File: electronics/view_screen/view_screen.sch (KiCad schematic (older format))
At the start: 12 parts, among them J1 Conn_01x04, J2 GC9A01, J3 Conn_01x04, J4 Conn_01x04, J5 Conn_01x04, Q1 2N7002

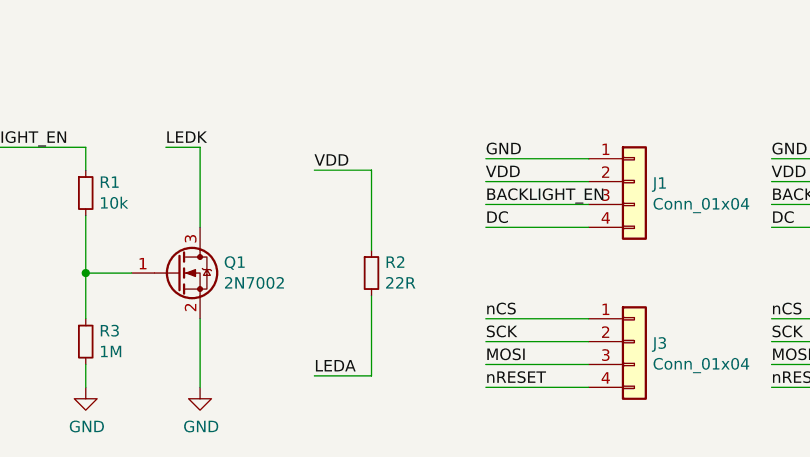
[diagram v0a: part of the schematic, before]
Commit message: Generate PCB assembly files
Generate assembly files for JLCPCB - BOM and CPL. Using existing LCSC part numbers (which may not be in the JLC part library), and positions/rotations are completely unverified, and of course many of the components are simply not available in any form in the JLC part library (e.g. TMC6300). Fixes #23.

Also changed LCD backlight resistor from 22 ohm to 20 ohm and added some additional part numbers for reference.
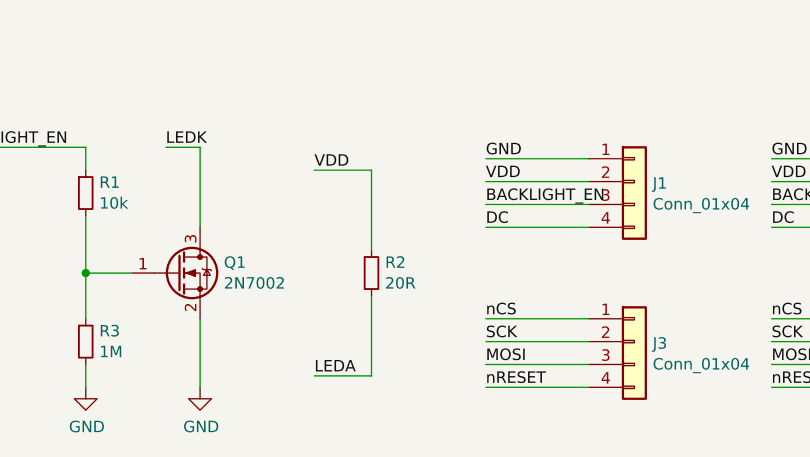
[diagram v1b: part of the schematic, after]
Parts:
- R2: value 22R -> 20R; Digikey RMCF0603JT22R0CT-ND -> RMCF0603JT20R0CT-ND; LCSC (none) -> C125758; Mouser 652-CR0603FX-22R0ELF -> 652-CR0603FX-20R0ELF
- R3: LCSC (none) -> C105578
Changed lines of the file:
@@
 F 4 "RMCF0603JT1M00CT-ND" H 3750 3550 50  0001 C CNN "Digikey"
 F 5 "652-CR0603FX-1004ELF" H 3750 3550 50  0001 C CNN "Mouser"
+F 6 "C105578" H 3750 3550 50  0001 C CNN "LCSC"
 	1    3750 3550
 	1    0    0    -1
@@
 P 5000 3250
 F 0 "R2" H 5059 3296 50  0000 L CNN
-F 1 "22R" H 5059 3205 50  0000 L CNN
+F 1 "20R" H 5059 3205 50  0000 L CNN
 F 2 "Resistor_SMD:R_0603_1608Metric" H 5000 3250 50  0001 C CNN
 F 3 "~" H 5000 3250 50  0001 C CNN
-F 4 "RMCF0603JT22R0CT-ND" H 5000 3250 50  0001 C CNN "Digikey"
-F 5 "652-CR0603FX-22R0ELF" H 5000 3250 50  0001 C CNN "Mouser"
+F 4 "RMCF0603JT20R0CT-ND" H 5000 3250 50  0001 C CNN "Digikey"
+F 5 "652-CR0603FX-20R0ELF" H 5000 3250 50  0001 C CNN "Mouser"
+F 6 "C125758" H 5000 3250 50  0001 C CNN "LCSC"
 	1    5000 3250
 	1    0    0    -1
